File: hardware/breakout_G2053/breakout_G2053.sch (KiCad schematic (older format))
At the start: 2 parts

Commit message: WIP schematic definition
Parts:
- added C?: 2.2u, SquantorRcl:C_0805, symbol Device:C_Small
- added J?: Conn_02x06_Odd_Even, symbol Connector_Generic:Conn_02x06_Odd_Even
- added R? (x4): TBD, SquantorRcl:R_1206, symbol Device:R
- added U?: G2053, symbol SquantorGmt:G2053
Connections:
- new net: C?.2, U?.14 (VINT)
- new net: R?.1, R?.1, U?.3 (AISEN)
- new net: R?.1, R?.1, U?.6 (BISEN)
- new net MOTOR_VDD: J?.1 (Pin_1), J?.2 (Pin_2), U?.12 (Vm)
- new net OUT1: J?.3 (Pin_3), J?.4 (Pin_4), U?.2 (AOUT1)
- new net OUT2: J?.5 (Pin_5), J?.6 (Pin_6), U?.4 (AOUT2)
- new net OUT3: J?.7 (Pin_7), J?.8 (Pin_8), U?.5 (BOUT2)
- new net OUT4: J?.10 (Pin_10), J?.9 (Pin_9), U?.7 (BOUT1)
- new net VSS: C?.1, J?.11 (Pin_11), J?.12 (Pin_12), R?.2, R?.2, R?.2, R?.2, U?.13 (GND), U?.17 (GND)
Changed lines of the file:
@@
 	1    0    0    -1
 $EndComp
+$Comp
+L SquantorGmt:G2053 U?
+U 1 1 5ED52BF7
+P 3850 2400
+F 0 "U?" H 3850 3115 50  0000 C CNN
+F 1 "G2053" H 3850 3024 50  0000 C CNN
+F 2 "" H 3850 2400 50  0001 C CNN
+F 3 "" H 3850 2400 50  0001 C CNN
+	1    3850 2400
+	1    0    0    -1
+$EndComp
+$Comp
+L Connector_Generic:Conn_02x06_Odd_Even J?
+U 1 1 5ED5359D
+P 1350 2450
+F 0 "J?" H 1400 2867 50  0000 C CNN
+F 1 "Conn_02x06_Odd_Even" H 1400 2776 50  0000 C CNN
+F 2 "" H 1350 2450 50  0001 C CNN
+F 3 "~" H 1350 2450 50  0001 C CNN
+	1    1350 2450
+	1    0    0    -1
+$EndComp
+Wire Wire Line
+	1150 2250 1100 2250
+Text Label 1100 2250 2    50   ~ 0
+MOTOR_VDD
+Text Label 1700 2250 0    50   ~ 0
+MOTOR_VDD
+Text Label 1100 2750 2    50   ~ 0
+VSS
+Text Label 1700 2750 0    50   ~ 0
+VSS
+Text Label 1100 2350 2    50   ~ 0
+OUT1
+Text Label 1100 2450 2    50   ~ 0
+OUT2
+Text Label 1100 2550 2    50   ~ 0
+OUT3
+Text Label 1100 2650 2    50   ~ 0
+OUT4
+Text Label 1700 2350 0    50   ~ 0
+OUT1
+Text Label 1700 2450 0    50   ~ 0
+OUT2
+Text Label 1700 2550 0    50   ~ 0
+OUT3
+Text Label 1700 2650 0    50   ~ 0
+OUT4
+Wire Wire Line
+	1150 2350 1100 2350
+Wire Wire Line
+	1100 2450 1150 2450
+Wire Wire Line
+	1150 2550 1100 2550
+Wire Wire Line
+	1100 2650 1150 2650
+Wire Wire Line
+	1150 2750 1100 2750
+Wire Wire Line
+	1650 2750 1700 2750
+Wire Wire Line
+	1700 2650 1650 2650
+Wire Wire Line
+	1650 2550 1700 2550
+Wire Wire Line
+	1700 2450 1650 2450
+Wire Wire Line
+	1650 2350 1700 2350
+Wire Wire Line
+	1700 2250 1650 2250
+$Comp
+L Device:C_Small C?
+U 1 1 5ED569B5
+P 4450 2250
+F 0 "C?" V 4400 2150 50  0000 C CNN
+F 1 "2.2u" V 4500 2350 50  0000 C CNN
+F 2 "SquantorRcl:C_0805" H 4450 2250 50  0001 C CNN
+F 3 "~" H 4450 2250 50  0001 C CNN
+	1    4450 2250
+	0    1    1    0
+$EndComp
+Text Label 4650 2250 0    50   ~ 0
+VSS
+Wire Wire Line
+	4300 2250 4350 2250
+Wire Wire Line
+	4550 2250 4650 2250
+Text Label 4650 1950 0    50   ~ 0
+VSS
+Text Label 4650 2350 0    50   ~ 0
+VSS
+Wire Wire Line
+	4300 1950 4650 1950
+Wire Wire Line
+	4650 2350 4300 2350
+Text Label 4650 2450 0    50   ~ 0
+MOTOR_VDD
+Wire Wire Line
+	4300 2450 4650 2450
+$Comp
+L Device:R R?
+U 1 1 5ED5D245
+P 2950 2200
+F 0 "R?" V 2900 2050 50  0000 C CNN
+F 1 "TBD" V 2950 2200 50  0000 C CNN
+F 2 "SquantorRcl:R_1206" V 2880 2200 50  0001 C CNN
+F 3 "~" H 2950 2200 50  0001 C CNN
+	1    2950 2200
+	0    1    1    0
+$EndComp
+Text Label 3350 2150 2    50   ~ 0
+OUT1
+Text Label 3350 2350 2    50   ~ 0
+OUT2
+Text Label 3350 2450 2    50   ~ 0
+OUT3
+Text Label 3350 2650 2    50   ~ 0
+OUT4
+$Comp
+L Device:R R?
+U 1 1 5ED5EEDE
+P 2950 2300
+F 0 "R?" V 2900 2150 50  0000 C CNN
+F 1 "TBD" V 2950 2300 50  0000 C CNN
+F 2 "SquantorRcl:R_1206" V 2880 2300 50  0001 C CNN
+F 3 "~" H 2950 2300 50  0001 C CNN
+	1    2950 2300
+	0    1    1    0
+$EndComp
+Text Label 2700 2250 2    50   ~ 0
+VSS
+Wire Wire Line
+	2800 2200 2750 2200
+Wire Wire Line
+	2750 2200 2750 2250
+Wire Wire Line
+	2750 2300 2800 2300
+Wire Wire Line
+	3100 2200 3150 2200
+Wire Wire Line
+	3150 2200 3150 2250
+Wire Wire Line
+	3150 2300 3100 2300
+Wire Wire Line
+	3150 2250 3400 2250
+Connection ~ 3150 2250
+Wire Wire Line
+	3150 2250 3150 2300
+Wire Wire Line
+	2750 2250 2700 2250
+Connection ~ 2750 2250
+Wire Wire Line
+	2750 2250 2750 2300
+$Comp
+L Device:R R?
+U 1 1 5ED6177F
+P 2950 2500
+F 0 "R?" V 2900 2350 50  0000 C CNN
+F 1 "TBD" V 2950 2500 50  0000 C CNN
+F 2 "SquantorRcl:R_1206" V 2880 2500 50  0001 C CNN
+F 3 "~" H 2950 2500 50  0001 C CNN
+	1    2950 2500
+	0    1    1    0
+$EndComp
+$Comp
+L Device:R R?
+U 1 1 5ED61789
+P 2950 2600
+F 0 "R?" V 2900 2450 50  0000 C CNN
+F 1 "TBD" V 2950 2600 50  0000 C CNN
+F 2 "SquantorRcl:R_1206" V 2880 2600 50  0001 C CNN
+F 3 "~" H 2950 2600 50  0001 C CNN
+	1    2950 2600
+	0    1    1    0
+$EndComp
+Text Label 2700 2550 2    50   ~ 0
+VSS
+Wire Wire Line
+	2800 2500 2750 2500
+Wire Wire Line
+	2750 2500 2750 2550
+Wire Wire Line
+	2750 2600 2800 2600
+Wire Wire Line
+	3100 2500 3150 2500
+Wire Wire Line
+	3150 2500 3150 2550
+Wire Wire Line
+	3150 2600 3100 2600
+Wire Wire Line
+	3150 2550 3400 2550
+Connection ~ 3150 2550
+Wire Wire Line
+	3150 2550 3150 2600
+Wire Wire Line
+	2750 2550 2700 2550
+Connection ~ 2750 2550
+Wire Wire Line
+	2750 2550 2750 2600
+Wire Wire Line
+	3400 2150 3350 2150
+Wire Wire Line
+	3350 2350 3400 2350
+Wire Wire Line
+	3400 2450 3350 2450
+Wire Wire Line
+	3350 2650 3400 2650
 $EndSCHEMATC

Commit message: WIP schematic and layout
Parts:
- J1: renamed from J?; footprint (none) -> Connector_PinHeader_2.54mm:PinHeader_2x06_P2.54mm_Vertical
- N2: footprint SquantorLabels:Label_version -> SquantorLabels:Label_Generic
- U1: renamed from U?; footprint (none) -> SquantorIC:TSSOP-16_EP
- gave numbers to parts that had none: 5
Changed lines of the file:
@@
 F 0 "N2" H 850 7800 60  0000 C CNN
 F 1 "20200601" H 850 7700 60  0000 C CNN
-F 2 "SquantorLabels:Label_version" H 850 7700 60  0001 C CNN
+F 2 "SquantorLabels:Label_Generic" H 850 7700 60  0001 C CNN
 F 3 "" H 850 7700 60  0001 C CNN
 	1    850  7700
@@
 $EndComp
 $Comp
-L SquantorGmt:G2053 U?
+L SquantorGmt:G2053 U1
 U 1 1 5ED52BF7
 P 3850 2400
-F 0 "U?" H 3850 3115 50  0000 C CNN
+F 0 "U1" H 3850 3115 50  0000 C CNN
 F 1 "G2053" H 3850 3024 50  0000 C CNN
-F 2 "" H 3850 2400 50  0001 C CNN
+F 2 "SquantorIC:TSSOP-16_EP" H 3850 2400 50  0001 C CNN
 F 3 "" H 3850 2400 50  0001 C CNN
 	1    3850 2400
@@
 $EndComp
 $Comp
-L Connector_Generic:Conn_02x06_Odd_Even J?
+L Connector_Generic:Conn_02x06_Odd_Even J1
 U 1 1 5ED5359D
 P 1350 2450
-F 0 "J?" H 1400 2867 50  0000 C CNN
+F 0 "J1" H 1400 2867 50  0000 C CNN
 F 1 "Conn_02x06_Odd_Even" H 1400 2776 50  0000 C CNN
-F 2 "" H 1350 2450 50  0001 C CNN
+F 2 "Connector_PinHeader_2.54mm:PinHeader_2x06_P2.54mm_Vertical" H 1350 2450 50  0001 C CNN
 F 3 "~" H 1350 2450 50  0001 C CNN
 	1    1350 2450
@@
 	1700 2250 1650 2250
 $Comp
-L Device:C_Small C?
+L Device:C_Small C1
 U 1 1 5ED569B5
 P 4450 2250
-F 0 "C?" V 4400 2150 50  0000 C CNN
+F 0 "C1" V 4400 2150 50  0000 C CNN
 F 1 "2.2u" V 4500 2350 50  0000 C CNN
 F 2 "SquantorRcl:C_0805" H 4450 2250 50  0001 C CNN
@@
 	4300 2450 4650 2450
 $Comp
-L Device:R R?
+L Device:R R1
 U 1 1 5ED5D245
 P 2950 2200
-F 0 "R?" V 2900 2050 50  0000 C CNN
+F 0 "R1" V 2900 2050 50  0000 C CNN
 F 1 "TBD" V 2950 2200 50  0000 C CNN
 F 2 "SquantorRcl:R_1206" V 2880 2200 50  0001 C CNN
@@
 OUT4
 $Comp
-L Device:R R?
+L Device:R R2
 U 1 1 5ED5EEDE
 P 2950 2300
-F 0 "R?" V 2900 2150 50  0000 C CNN
+F 0 "R2" V 2900 2150 50  0000 C CNN
 F 1 "TBD" V 2950 2300 50  0000 C CNN
 F 2 "SquantorRcl:R_1206" V 2880 2300 50  0001 C CNN
@@
 	2750 2250 2750 2300
 $Comp
-L Device:R R?
+L Device:R R3
 U 1 1 5ED6177F
 P 2950 2500
-F 0 "R?" V 2900 2350 50  0000 C CNN
+F 0 "R3" V 2900 2350 50  0000 C CNN
 F 1 "TBD" V 2950 2500 50  0000 C CNN
 F 2 "SquantorRcl:R_1206" V 2880 2500 50  0001 C CNN
@@
 $EndComp
 $Comp
-L Device:R R?
+L Device:R R4
 U 1 1 5ED61789
 P 2950 2600
-F 0 "R?" V 2900 2450 50  0000 C CNN
+F 0 "R4" V 2900 2450 50  0000 C CNN
 F 1 "TBD" V 2950 2600 50  0000 C CNN
 F 2 "SquantorRcl:R_1206" V 2880 2600 50  0001 C CNN

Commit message: further modifications of schematic
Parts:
- added C2: 10u, SquantorRcl:C_0805, symbol Device:C_Small
- added R5, R6: 4.7K, SquantorRcl:R_0603_hand, symbol Device:R
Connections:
- net MOTOR_VDD: now also C2.2
- net OUT1: no longer U1.2 (AOUT1)
- net OUT2: no longer U1.4 (AOUT2)
- net OUT3: no longer U1.5 (BOUT2)
- net OUT4: no longer U1.7 (BOUT1)
- net VSS: now also C2.1
- net nSLEEP: now reaches U1.1 (nSLEEP)
- net nSLEEP: now also R5.2
- net BIN2: now reaches U1.10 (BIN2)
- net AIN2: now reaches U1.15 (AIN2)
- net AIN1: now reaches U1.16 (AIN1)
- net nFAULT: now reaches U1.8 (nFAULT)
- net nFAULT: now also R6.2
- net BIN1: now reaches U1.9 (BIN1)
- new net AOUT1: U1.2 (AOUT1)
- new net AOUT2: U1.4 (AOUT2)
- new net BOUT1: U1.7 (BOUT1)
- new net BOUT2: U1.5 (BOUT2)
- new net VDD: R5.1, R6.1
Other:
- moved on the sheet: R1, R2, R3, R4

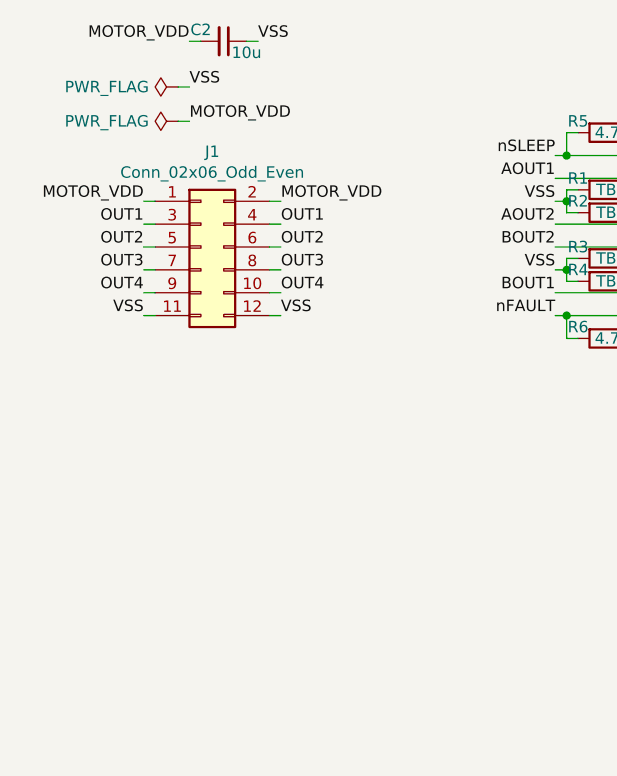
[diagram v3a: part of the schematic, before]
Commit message: WIP further schematic definition, input connector
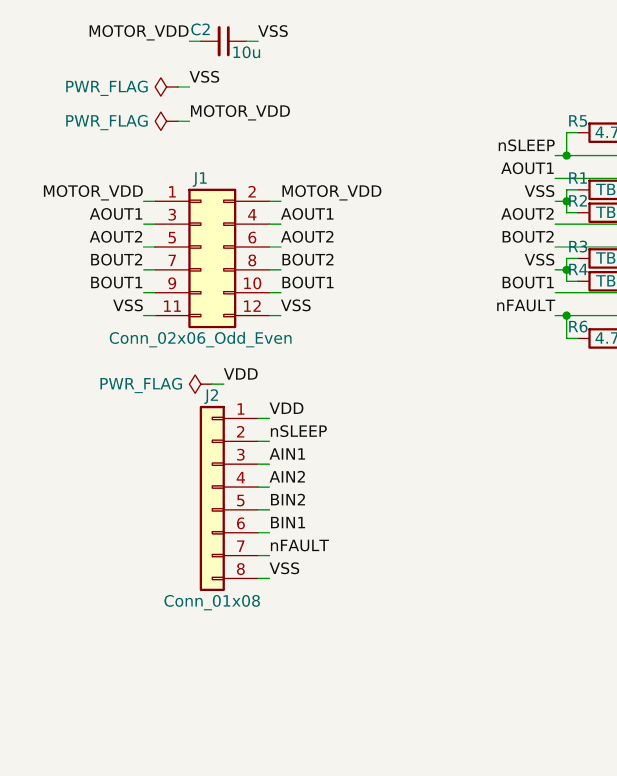
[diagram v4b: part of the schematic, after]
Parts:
- added J2: Conn_01x08, Connector_PinHeader_2.54mm:PinHeader_1x08_P2.54mm_Vertical, symbol Connector_Generic:Conn_01x08
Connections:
- net OUT1 is gone; now on net AOUT1: J1.3 (Pin_3), J1.4 (Pin_4)
- net OUT2 is gone; now on net AOUT2: J1.5 (Pin_5), J1.6 (Pin_6)
- net OUT3 is gone; now on net BOUT2: J1.7 (Pin_7), J1.8 (Pin_8)
- net OUT4 is gone; now on net BOUT1: J1.10 (Pin_10), J1.9 (Pin_9)
- net AIN1: now also J2.3 (Pin_3)
- net AIN2: now also J2.4 (Pin_4)
- net BIN1: now also J2.6 (Pin_6)
- net BIN2: now also J2.5 (Pin_5)
- net VDD: now also J2.1 (Pin_1)
- net VSS: now also J2.8 (Pin_8)
- net nFAULT: now also J2.7 (Pin_7)
- net nSLEEP: now also J2.2 (Pin_2)
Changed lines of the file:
@@
 U 1 1 5ED5359D
 P 1350 2450
-F 0 "J1" H 1400 2867 50  0000 C CNN
-F 1 "Conn_02x06_Odd_Even" H 1400 2776 50  0000 C CNN
+F 0 "J1" H 1350 2750 50  0000 C CNN
+F 1 "Conn_02x06_Odd_Even" H 1350 2050 50  0000 C CNN
 F 2 "Connector_PinHeader_2.54mm:PinHeader_2x06_P2.54mm_Vertical" H 1350 2450 50  0001 C CNN
 F 3 "~" H 1350 2450 50  0001 C CNN
@@
 Text Label 1700 2750 0    50   ~ 0
 VSS
-Text Label 1100 2350 2    50   ~ 0
-OUT1
-Text Label 1100 2450 2    50   ~ 0
-OUT2
-Text Label 1100 2550 2    50   ~ 0
-OUT3
-Text Label 1100 2650 2    50   ~ 0
-OUT4
-Text Label 1700 2350 0    50   ~ 0
-OUT1
-Text Label 1700 2450 0    50   ~ 0
-OUT2
-Text Label 1700 2550 0    50   ~ 0
-OUT3
-Text Label 1700 2650 0    50   ~ 0
-OUT4
 Wire Wire Line
 	1150 2350 1100 2350
@@
 Wire Wire Line
 	1550 1550 1600 1550
+$Comp
+L Connector_Generic:Conn_01x08 J2
+U 1 1 5EE01BD6
+P 1400 3500
+F 0 "J2" H 1400 3900 50  0000 C CNN
+F 1 "Conn_01x08" H 1400 3000 50  0000 C CNN
+F 2 "Connector_PinHeader_2.54mm:PinHeader_1x08_P2.54mm_Vertical" H 1400 3500 50  0001 C CNN
+F 3 "~" H 1400 3500 50  0001 C CNN
+	1    1400 3500
+	-1   0    0    -1
+$EndComp
+Text Label 1650 3200 0    50   ~ 0
+VDD
+Text Label 1650 3900 0    50   ~ 0
+VSS
+Text Label 1650 3800 0    50   ~ 0
+nFAULT
+Text Label 1650 3700 0    50   ~ 0
+BIN1
+Text Label 1650 3600 0    50   ~ 0
+BIN2
+Text Label 1650 3500 0    50   ~ 0
+AIN2
+Text Label 1650 3400 0    50   ~ 0
+AIN1
+Text Label 1650 3300 0    50   ~ 0
+nSLEEP
+Wire Wire Line
+	1600 3200 1650 3200
+Wire Wire Line
+	1650 3300 1600 3300
+Wire Wire Line
+	1600 3400 1650 3400
+Wire Wire Line
+	1650 3500 1600 3500
+Wire Wire Line
+	1600 3600 1650 3600
+Wire Wire Line
+	1650 3700 1600 3700
+Wire Wire Line
+	1600 3800 1650 3800
+Wire Wire Line
+	1650 3900 1600 3900
+$Comp
+L power:PWR_FLAG #FLG0101
+U 1 1 5EE18E15
+P 1400 3050
+F 0 "#FLG0101" H 1400 3125 50  0001 C CNN
+F 1 "PWR_FLAG" V 1400 3177 50  0000 L CNN
+F 2 "" H 1400 3050 50  0001 C CNN
+F 3 "~" H 1400 3050 50  0001 C CNN
+	1    1400 3050
+	0    -1   -1   0
+$EndComp
+Text Label 1450 3050 0    50   ~ 0
+VDD
+Wire Wire Line
+	1400 3050 1450 3050
+Text Label 1700 2350 0    50   ~ 0
+AOUT1
+Text Label 1700 2450 0    50   ~ 0
+AOUT2
+Text Label 1700 2550 0    50   ~ 0
+BOUT2
+Text Label 1700 2650 0    50   ~ 0
+BOUT1
+Text Label 1100 2350 2    50   ~ 0
+AOUT1
+Text Label 1100 2450 2    50   ~ 0
+AOUT2
+Text Label 1100 2550 2    50   ~ 0
+BOUT2
+Text Label 1100 2650 2    50   ~ 0
+BOUT1
 $EndSCHEMATC

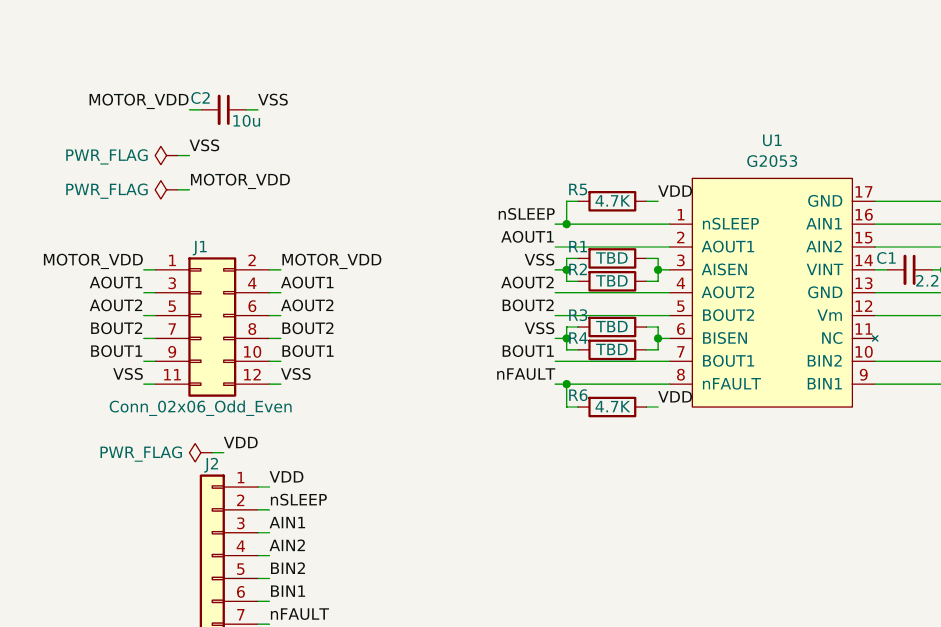
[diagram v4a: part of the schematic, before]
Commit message: added indication leds
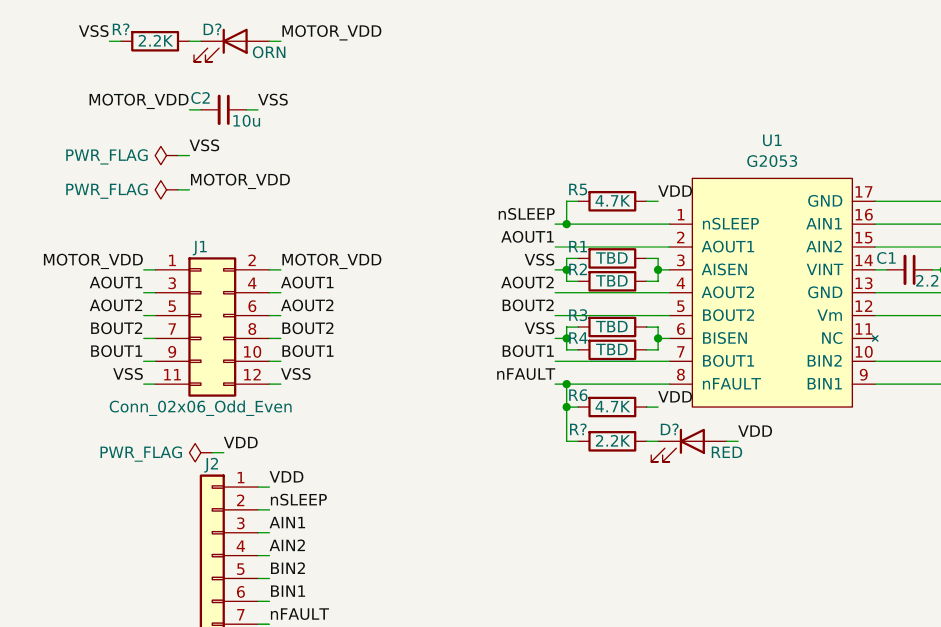
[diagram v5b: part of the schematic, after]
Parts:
- added D?: RED, SquantorDiodes:LED_0603_hand, symbol Device:LED
- added D?: ORN, SquantorDiodes:LED_0603_hand, symbol Device:LED
- added R? (x2): 2.2K, SquantorRcl:R_0603_hand, symbol Device:R
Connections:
- net MOTOR_VDD: now also D?.2 (A)
- net VDD: now also D?.2 (A)
- net VSS: now also R?.2
- net nFAULT: now also R?.2
- new net: D?.1 (K), R?.1 (x2)
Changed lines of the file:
@@
 Text Label 1100 2650 2    50   ~ 0
 BOUT1
+$Comp
+L Device:R R?
+U 1 1 5EE24C63
+P 3150 3000
+F 0 "R?" V 3100 2850 50  0000 C CNN
+F 1 "2.2K" V 3150 3000 50  0000 C CNN
+F 2 "SquantorRcl:R_0603_hand" V 3080 3000 50  0001 C CNN
+F 3 "~" H 3150 3000 50  0001 C CNN
+	1    3150 3000
+	0    1    1    0
+$EndComp
+$Comp
+L Device:LED D?
+U 1 1 5EE258E7
+P 3500 3000
+F 0 "D?" H 3400 3050 50  0000 C CNN
+F 1 "RED" H 3650 2950 50  0000 C CNN
+F 2 "SquantorDiodes:LED_0603_hand" H 3500 3000 50  0001 C CNN
+F 3 "~" H 3500 3000 50  0001 C CNN
+	1    3500 3000
+	1    0    0    -1
+$EndComp
+Text Label 3700 3000 0    50   ~ 0
+VDD
+Wire Wire Line
+	2950 2850 2950 3000
+Wire Wire Line
+	2950 3000 3000 3000
+Connection ~ 2950 2850
+Wire Wire Line
+	3300 3000 3350 3000
+Wire Wire Line
+	3650 3000 3700 3000
+$Comp
+L Device:R R?
+U 1 1 5EE2D78F
+P 1150 1250
+F 0 "R?" V 1100 1100 50  0000 C CNN
+F 1 "2.2K" V 1150 1250 50  0000 C CNN
+F 2 "SquantorRcl:R_0603_hand" V 1080 1250 50  0001 C CNN
+F 3 "~" H 1150 1250 50  0001 C CNN
+	1    1150 1250
+	0    1    1    0
+$EndComp
+$Comp
+L Device:LED D?
+U 1 1 5EE2E712
+P 1500 1250
+F 0 "D?" H 1400 1300 50  0000 C CNN
+F 1 "ORN" H 1650 1200 50  0000 C CNN
+F 2 "SquantorDiodes:LED_0603_hand" H 1500 1250 50  0001 C CNN
+F 3 "~" H 1500 1250 50  0001 C CNN
+	1    1500 1250
+	1    0    0    -1
+$EndComp
+Text Label 1700 1250 0    50   ~ 0
+MOTOR_VDD
+Text Label 950  1250 2    50   ~ 0
+VSS
+Wire Wire Line
+	1650 1250 1700 1250
+Wire Wire Line
+	1350 1250 1300 1250
+Wire Wire Line
+	1000 1250 950  1250
 $EndSCHEMATC

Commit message: ERC passed!
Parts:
- gave numbers to parts that had none: 4
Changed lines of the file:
@@
 BOUT1
 $Comp
-L Device:R R?
+L Device:R R8
 U 1 1 5EE24C63
 P 3150 3000
-F 0 "R?" V 3100 2850 50  0000 C CNN
+F 0 "R8" V 3100 2850 50  0000 C CNN
 F 1 "2.2K" V 3150 3000 50  0000 C CNN
 F 2 "SquantorRcl:R_0603_hand" V 3080 3000 50  0001 C CNN
@@
 $EndComp
 $Comp
-L Device:LED D?
+L Device:LED D2
 U 1 1 5EE258E7
 P 3500 3000
-F 0 "D?" H 3400 3050 50  0000 C CNN
+F 0 "D2" H 3400 3050 50  0000 C CNN
 F 1 "RED" H 3650 2950 50  0000 C CNN
 F 2 "SquantorDiodes:LED_0603_hand" H 3500 3000 50  0001 C CNN
@@
 	3650 3000 3700 3000
 $Comp
-L Device:R R?
+L Device:R R7
 U 1 1 5EE2D78F
 P 1150 1250
-F 0 "R?" V 1100 1100 50  0000 C CNN
+F 0 "R7" V 1100 1100 50  0000 C CNN
 F 1 "2.2K" V 1150 1250 50  0000 C CNN
 F 2 "SquantorRcl:R_0603_hand" V 1080 1250 50  0001 C CNN
@@
 $EndComp
 $Comp
-L Device:LED D?
+L Device:LED D1
 U 1 1 5EE2E712
 P 1500 1250
-F 0 "D?" H 1400 1300 50  0000 C CNN
+F 0 "D1" H 1400 1300 50  0000 C CNN
 F 1 "ORN" H 1650 1200 50  0000 C CNN
 F 2 "SquantorDiodes:LED_0603_hand" H 1500 1250 50  0001 C CNN

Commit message: WIP routing/silk placement
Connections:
- net MOTOR_VDD: now also J1.11 (Pin_11), J1.12 (Pin_12); no longer J1.1 (Pin_1), J1.2 (Pin_2)
- net VSS: now also J1.1 (Pin_1), J1.2 (Pin_2); no longer J1.11 (Pin_11), J1.12 (Pin_12)
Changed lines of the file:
@@
 Wire Wire Line
 	1150 2250 1100 2250
+Text Label 1100 2750 2    50   ~ 0
+MOTOR_VDD
+Text Label 1700 2750 0    50   ~ 0
+MOTOR_VDD
 Text Label 1100 2250 2    50   ~ 0
-MOTOR_VDD
+VSS
 Text Label 1700 2250 0    50   ~ 0
-MOTOR_VDD
-Text Label 1100 2750 2    50   ~ 0
-VSS
-Text Label 1700 2750 0    50   ~ 0
 VSS
 Wire Wire Line

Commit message: updated versionnumber
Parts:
- N2: value 20200601 -> 20200605
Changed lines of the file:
@@
 P 850 7700
 F 0 "N2" H 850 7800 60  0000 C CNN
-F 1 "20200601" H 850 7700 60  0000 C CNN
+F 1 "20200605" H 850 7700 60  0000 C CNN
 F 2 "SquantorLabels:Label_Generic" H 850 7700 60  0001 C CNN
 F 3 "" H 850 7700 60  0001 C CNN
